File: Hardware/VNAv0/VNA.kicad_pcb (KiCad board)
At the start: 4 copper layers, 100 x 66 mm, 254 parts, among them J1 USB_B_Micro, J2 USB_A, J3 Conn_ARM_SWD, J4 SMA, J5 SMA, J6 UART, Q1 RE1C002UN, SW1 SW_Push, SW2 SW_Push, SW3 SW_Push, U1 TPD2S017, U10 74AHC1G04, U11 PE42440, U12 SN74LVC1G139, U13 PE42440, U14 F2923, U15 AD8302, U16 STM32F373RCTx, U17 AT25SF081-SSHD-X, U2 TPD2S017, U3 MAX2871, U4 LP5912, U5 LP5912, U6 MIC5366-1.8, U7 AD8319, U8 SKY12347-362LF, U9 TRF37A75, X1 ASTXR-12-19.200MHz, Y1 8MHz

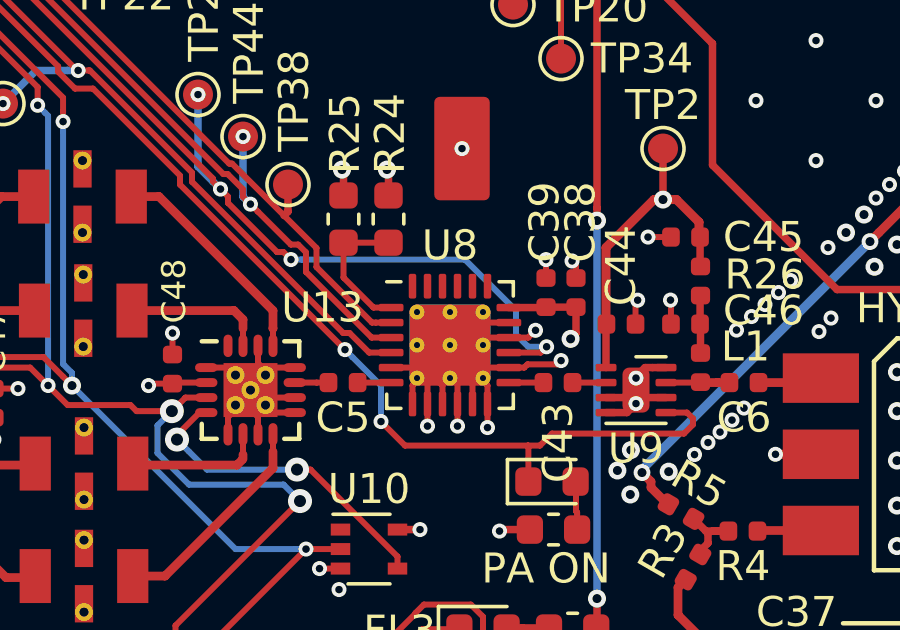
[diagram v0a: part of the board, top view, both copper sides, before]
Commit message: tx chain now works, however output power too low
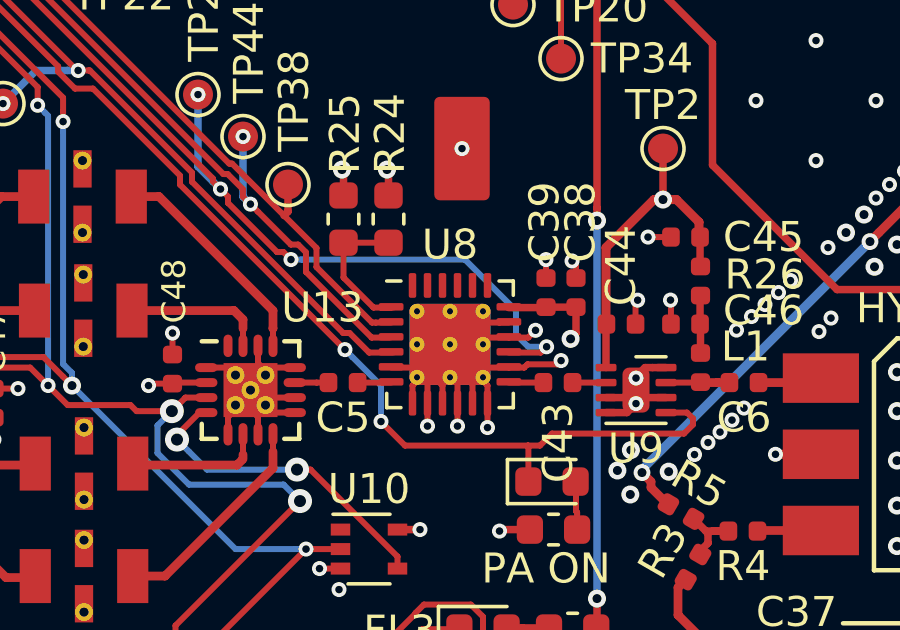
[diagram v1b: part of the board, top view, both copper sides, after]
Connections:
- J1 pad 4: (no net) -> Net-(J1-Pad4)
- J3 pad 6: (no net) -> Net-(J3-Pad6)
- J3 pad 7: (no net) -> Net-(J3-Pad7)
- J3 pad 8: (no net) -> Net-(J3-Pad8)
- U16 pad 1: (no net) -> Net-(U16-Pad1)
- U16 pad 26: (no net) -> /Microcontroller/SDADC_AIN6P
- U16 pad 47: (no net) -> Net-(U16-Pad47)
- U16 pad 48: (no net) -> Net-(U16-Pad48)
- U16 pad 51: (no net) -> Net-(U16-Pad51)
- U8 pad 19: (no net) -> Net-(U8-Pad19)
- U8 pad 20: (no net) -> Net-(U8-Pad20)
- U8 pad 21: (no net) -> Net-(U8-Pad21)
- U8 pad 22: (no net) -> Net-(U8-Pad22)
- U8 pad 23: (no net) -> Net-(U8-Pad23)
- U8 pad 24: (no net) -> Net-(U8-Pad24)
